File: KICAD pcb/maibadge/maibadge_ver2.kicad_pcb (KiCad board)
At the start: 2 copper layers, 62.5 x 97.2 mm, 22 parts, among them J1 Conn_01x04_Socket, SW1 SW_Push, SW2 SW_Push, SW3 SW_Push, SW4 SW_Push, U1 ESP32-S3-WROOM-1, U10 SK6812SIDE-A-RVS, U2 AMS1117-3.3, U3 SK6812SIDE-A-RVS, U4 SK6812SIDE-A-RVS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

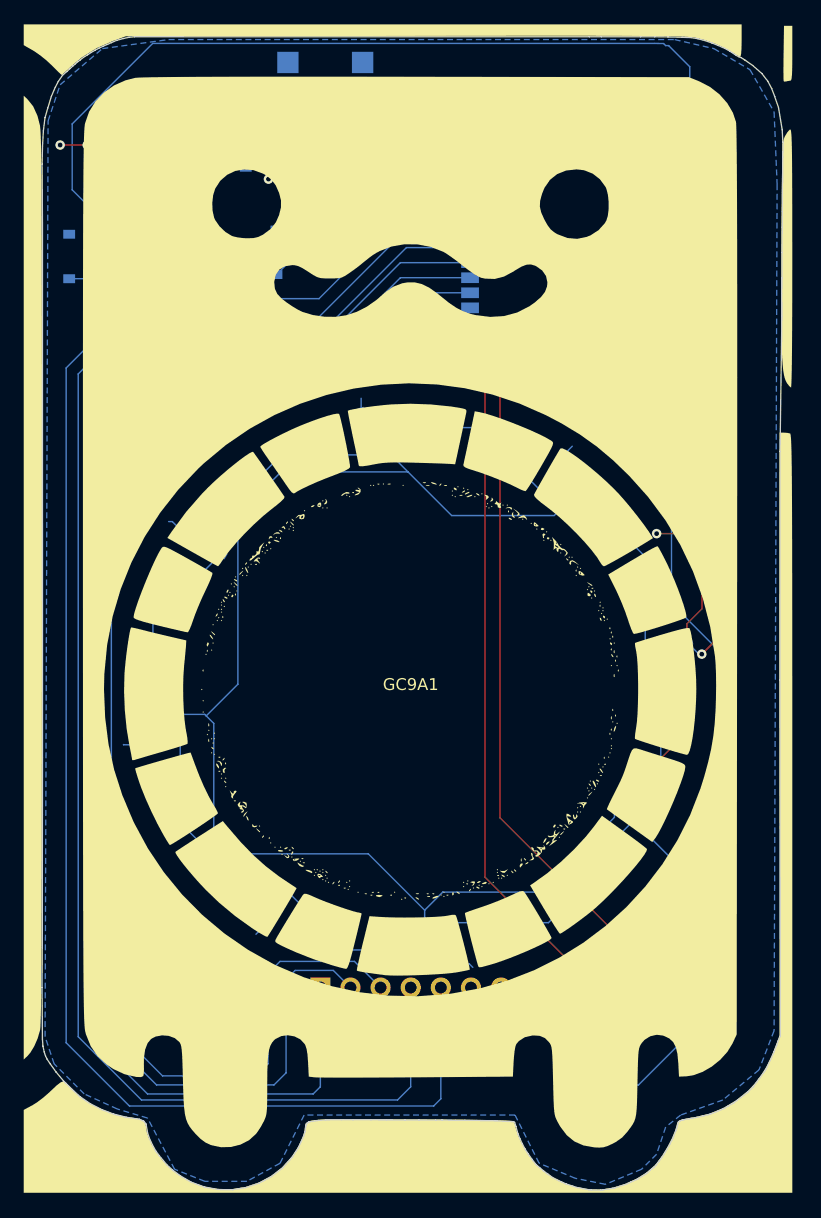
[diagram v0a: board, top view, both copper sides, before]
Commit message: fix: silkscreen invert
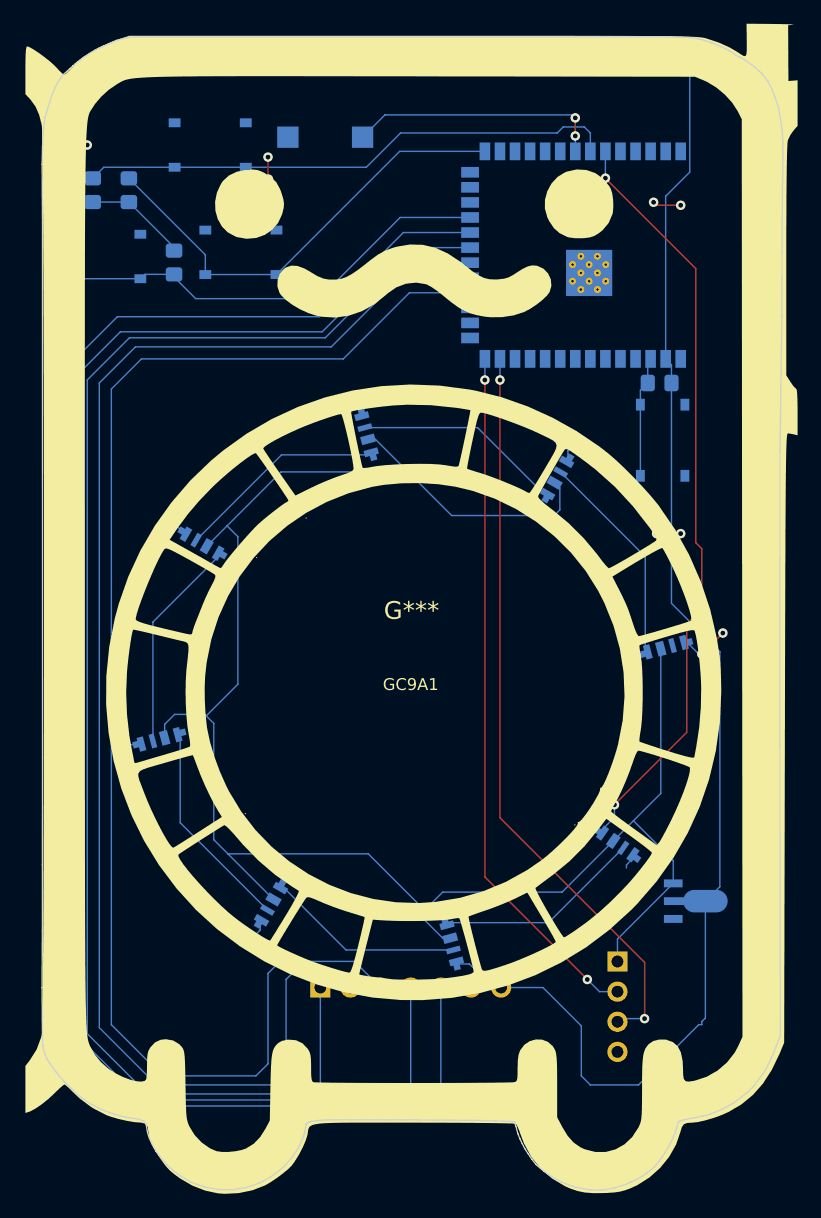
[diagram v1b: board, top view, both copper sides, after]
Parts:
- moved G*** 0.34 mm to (190.2, 86.8)

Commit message: fix: schematic and routing
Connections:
- J1 pad 1: +5V -> GND
- J1 pad 4: GND -> +5V
- U1 pad 24: /MPR SDA -> /buzzer
- U1 pad 25: /MPR SCL -> unconnected-(U1-IO48-Pad25)
- U1 pad 33: /buzzer -> unconnected-(U1-IO40-Pad33)
- U1 pad 35: /main led DIN -> unconnected-(U1-IO42-Pad35)
- U1 pad 8: unconnected-(U1-IO15-Pad8) -> /main led DIN
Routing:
- net /main led DIN: track 64.3 -> 52.5 mm
- net /buzzer: track 21.6 -> 11.4 mm
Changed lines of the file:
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@@
 	(net 21 "unconnected-(U1-IO35-Pad28)")
 	(net 22 "unconnected-(U1-IO36-Pad29)")
-	(net 23 "/MPR SCL")
+	(net 23 "unconnected-(U1-IO40-Pad33)")
 	(net 24 "unconnected-(U1-IO37-Pad30)")
 	(net 25 "unconnected-(U1-IO6-Pad6)")
@@
 	(net 35 "/OLED_CS")
 	(net 36 "unconnected-(U1-IO17-Pad10)")
-	(net 37 "/MPR SDA")
+	(net 37 "unconnected-(U1-IO42-Pad35)")
 	(net 38 "unconnected-(U1-IO3-Pad15)")
 	(net 39 "unconnected-(U1-IO7-Pad7)")
-	(net 40 "unconnected-(U1-IO15-Pad8)")
+	(net 40 "unconnected-(U1-IO48-Pad25)")
 	(net 41 "Net-(U3-DOUT)")
 	(net 42 "Net-(U4-DOUT)")
@@
 			(size 1.5 0.9)
 			(layers "B.Cu" "B.Paste" "B.Mask")
-			(net 40 "unconnected-(U1-IO15-Pad8)")
+			(net 28 "/main led DIN")
 			(pinfunction "IO15")
 			(pintype "bidirectional")
@@
 			(size 1.5 0.9)
 			(layers "B.Cu" "B.Paste" "B.Mask")
-			(net 37 "/MPR SDA")
+			(net 2 "/buzzer")
 			(pinfunction "IO47")
 			(pintype "bidirectional")
@@
 			(size 1.5 0.9)
 			(layers "B.Cu" "B.Paste" "B.Mask")
-			(net 23 "/MPR SCL")
+			(net 40 "unconnected-(U1-IO48-Pad25)")
 			(pinfunction "IO48")
 			(pintype "bidirectional")
@@
 			(size 1.5 0.9)
 			(layers "B.Cu" "B.Paste" "B.Mask")
-			(net 2 "/buzzer")
+			(net 23 "unconnected-(U1-IO40-Pad33)")
 			(pinfunction "IO40")
 			(pintype "bidirectional")
@@
 			(size 1.5 0.9)
 			(layers "B.Cu" "B.Paste" "B.Mask")
-			(net 28 "/main led DIN")
+			(net 37 "unconnected-(U1-IO42-Pad35)")
 			(pinfunction "IO42")
 			(pintype "bidirectional")
@@
 			(layers "*.Cu" "*.Mask")
 			(remove_unused_layers no)
-			(net 3 "+5V")
+			(net 1 "GND")
 			(pinfunction "Pin_1")
 			(pintype "passive")
@@
 			(layers "*.Cu" "*.Mask")
 			(remove_unused_layers no)
-			(net 1 "GND")
+			(net 3 "+5V")
 			(pinfunction "Pin_4")
 			(pintype "passive")
@@
 	)
 	(segment
-		(start 203.962 45.212)
-		(end 203.962 46.736)
+		(start 193.364184 52.073887)
+		(end 193.202129 52.073887)
+		(width 0.12)
+		(layer "F.Cu")
+		(net 2)
+	)
+	(segment
+		(start 193.202129 52.073887)
+		(end 187.95343 46.825188)
 		(width 0.12)
 		(layer "F.Cu")
@@
 	)
 	(via
-		(at 203.962 46.736)
+		(at 193.364184 52.073887)
 		(size 0.8)
 		(drill 0.4)
@@
 	)
 	(via
-		(at 203.962 45.212)
+		(at 187.95343 46.825188)
 		(size 0.8)
 		(drill 0.4)
@@
 	)
 	(segment
-		(start 203.962 46.736)
-		(end 203.962 48.031997)
+		(start 187.95343 46.825188)
+		(end 186.04278 46.825188)
 		(width 0.12)
 		(layer "B.Cu")
@@
 	)
 	(segment
-		(start 186.029983 46.837985)
-		(end 187.909968 44.958)
-		(width 0.12)
+		(start 193.627293 52.336996)
+		(end 193.364184 52.073887)
+		(width 0.254)
 		(layer "B.Cu")
 		(net 2)
 	)
 	(segment
-		(start 187.909968 44.958)
-		(end 203.708 44.958)
-		(width 0.12)
+		(start 195.091994 52.336996)
+		(end 193.627293 52.336996)
+		(width 0.254)
 		(layer "B.Cu")
 		(net 2)
 	)
 	(segment
-		(start 203.708 44.958)
-		(end 203.962 45.212)
+		(start 195.05795 52.336996)
+		(end 195.036623 52.315669)
+		(width 0.254)
+		(layer "B.Cu")
+		(net 2)
+	)
+	(segment
+		(start 195.091994 52.336996)
+		(end 195.05795 52.336996)
+		(width 0.254)
+		(layer "B.Cu")
+		(net 2)
+	)
+	(segment
+		(start 186.04278 46.825188)
+		(end 186.029983 46.837985)
 		(width 0.12)
 		(layer "B.Cu")
@@
 	)
 	(segment
-		(start 214.122 57.912)
-		(end 206.502 50.292)
+		(start 203.997053 63.193957)
+		(end 203.997053 63.236634)
+		(width 0.12)
+		(layer "F.Cu")
+		(net 28)
+	)
+	(segment
+		(start 214.122 73.361581)
+		(end 214.122 81.026)
 		(width 0.12)
 		(layer "F.Cu")
@@
 	(segment
 		(start 213.36 97.028)
-		(end 213.36 87.884)
+		(end 207.264 103.124)
 		(width 0.12)
 		(layer "F.Cu")
@@
 	)
 	(segment
-		(start 214.63 81.534)
-		(end 214.122 81.026)
+		(start 213.36 87.884)
+		(end 213.36 97.028)
 		(width 0.12)
 		(layer "F.Cu")
@@
 	(segment
 		(start 214.63 86.614)
-		(end 214.63 81.534)
+		(end 213.36 87.884)
 		(width 0.12)
 		(layer "F.Cu")
@@
 	(segment
 		(start 214.122 81.026)
-		(end 214.122 57.912)
+		(end 214.63 81.534)
 		(width 0.12)
 		(layer "F.Cu")
@@
 	)
 	(segment
-		(start 207.264 103.124)
-		(end 213.36 97.028)
+		(start 214.63 81.534)
+		(end 214.63 86.614)
 		(width 0.12)
 		(layer "F.Cu")
@@
 	)
 	(segment
-		(start 213.36 87.884)
-		(end 214.63 86.614)
+		(start 203.997053 63.236634)
+		(end 214.122 73.361581)
 		(width 0.12)
 		(layer "F.Cu")
@@
 	)
 	(via
-		(at 206.502 50.292)
+		(at 203.997053 63.193957)
 		(size 0.8)
 		(drill 0.4)
@@
 	)
 	(segment
-		(start 206.501995 50.291995)
-		(end 206.502 50.292)
-		(width 0.12)
+		(start 203.961992 63.229018)
+		(end 203.961992 65.531997)
+		(width 0.254)
 		(layer "B.Cu")
 		(net 28)
 	)
 	(segment
-		(start 207.264 103.124)
-		(end 207.264 104.189499)
-		(width 0.12)
+		(start 203.997053 63.193957)
+		(end 203.961992 63.229018)
+		(width 0.254)
 		(layer "B.Cu")
 		(net 28)
 	)
 	(segment
-		(start 207.264 104.189499)
-		(end 206.076436 105.377063)
+		(start 207.264 103.124)
+		(end 207.264 104.189499)
 		(width 0.12)
 		(layer "B.Cu")
@@
 	)
 	(segment
-		(start 206.501995 48.031998)
-		(end 206.501995 50.291995)
+		(start 207.264 104.189499)
+		(end 206.076436 105.377063)
 		(width 0.12)
 		(layer "B.Cu")
